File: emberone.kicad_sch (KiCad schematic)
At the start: 2 parts, among them J1 Screw Terminal, J2 Screw Terminal

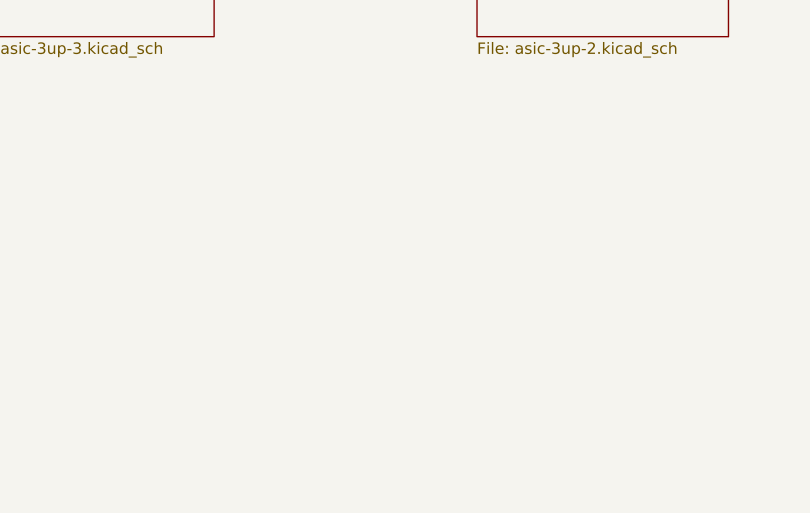
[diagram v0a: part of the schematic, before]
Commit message: added the heatsink mounting holes
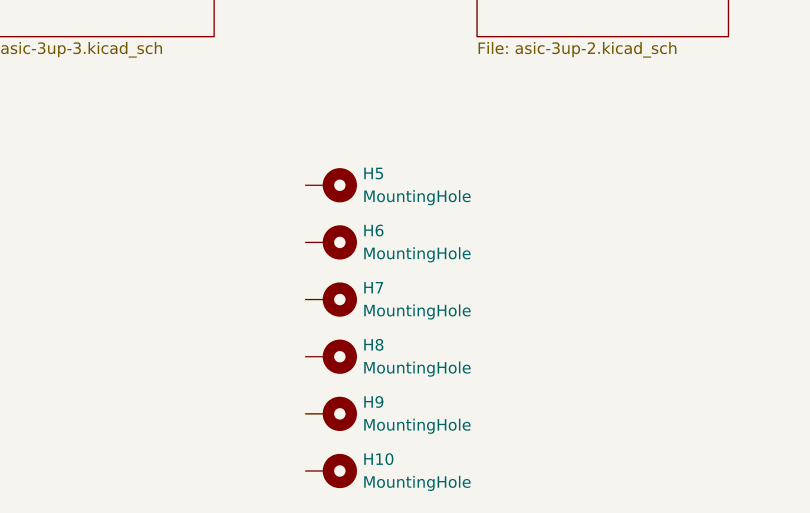
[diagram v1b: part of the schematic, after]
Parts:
- added H10, H5, H6, H7, H8, H9: MountingHole, MountingHole:MountingHole_3.2mm_M3_Pad, symbol Mechanical:MountingHole_Pad

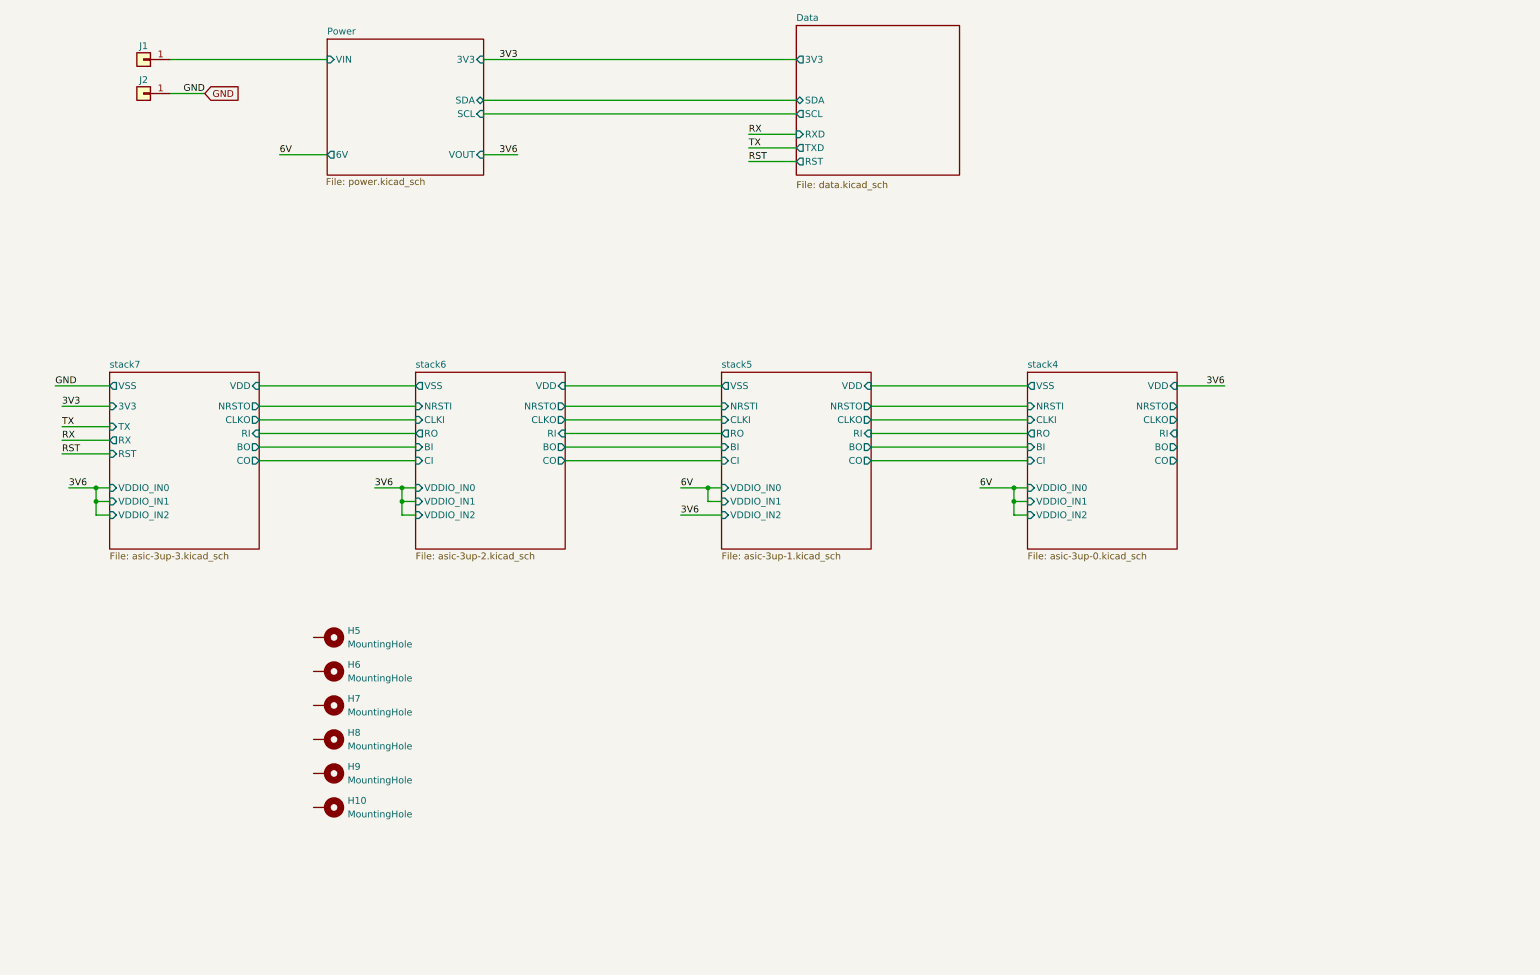
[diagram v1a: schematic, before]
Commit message: Switched to 5V for VDDIO LDO input.. cleaned up RP2040 circuit. Need to place and route testpoints
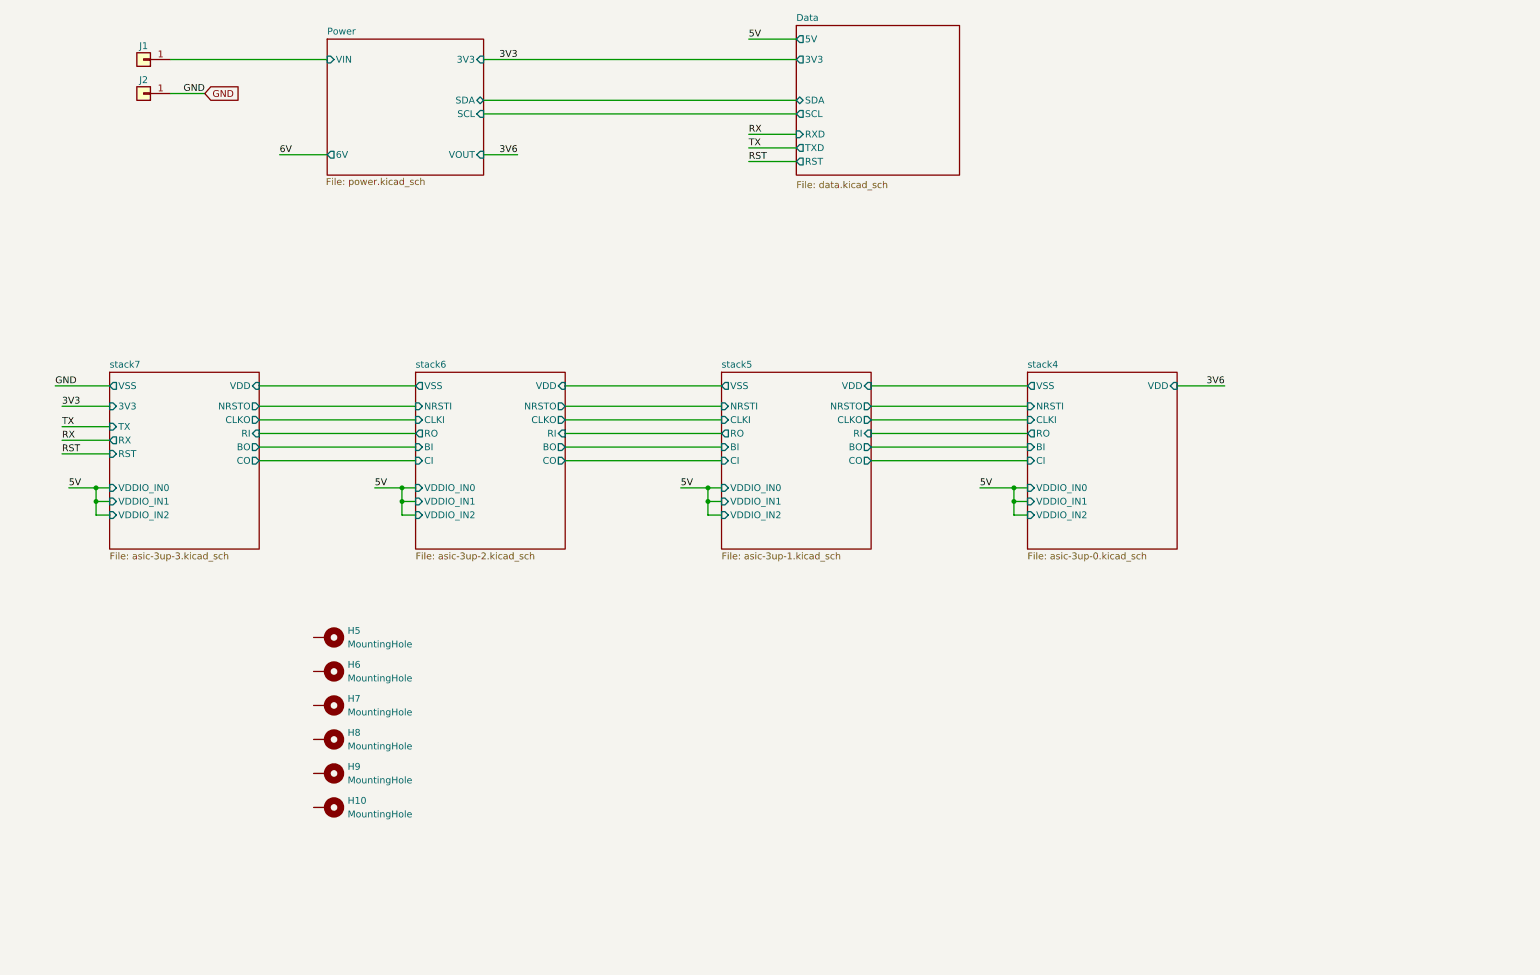
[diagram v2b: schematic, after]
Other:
- sheet Data ports: added 5V; removed none
- sheet stack4 ports: added none; removed BO, CLKO, CO, NRSTO, RI
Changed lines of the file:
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@@
+	)
+	(junction
+		(at 222.25 165.1)
+		(diameter 0)
+		(color 0 0 0 0)
 	)
 	(junction
@@
 	(wire
 		(pts
+			(xy 224.79 167.64) (xy 222.25 167.64)
+		)
+		(stroke
+			(width 0)
+			(type default)
+		)
+	)
+	(wire
+		(pts
 			(xy 229.87 101.6) (xy 238.76 101.6)
 		)
@@
 	(wire
 		(pts
+			(xy 222.25 167.64) (xy 222.25 165.1)
+		)
+		(stroke
+			(width 0)
+			(type default)
+		)
+	)
+	(wire
+		(pts
 			(xy 101.6 156.21) (xy 110.49 156.21)
 		)
@@
 	(wire
 		(pts
+			(xy 229.87 78.74) (xy 238.76 78.74)
+		)
+		(stroke
+			(width 0)
+			(type default)
+		)
+	)
+	(wire
+		(pts
 			(xy 121.92 82.55) (xy 151.13 82.55)
 		)
@@
 	(wire
 		(pts
-			(xy 217.17 167.64) (xy 224.79 167.64)
-		)
-		(stroke
-			(width 0)
-			(type default)
-		)
-	)
-	(wire
-		(pts
 			(xy 107.95 162.56) (xy 110.49 162.56)
 		)
@@
 		)
 	)
-	(label "GND"
-		(at 128.27 88.9 180)
+	(label "5V"
+		(at 160.02 162.56 0)
 		(fields_autoplaced yes)
 		(effects
@@
 				(size 1.27 1.27)
 			)
-			(justify right bottom)
-		)
-	)
-	(label "6V"
-		(at 217.17 162.56 0)
+			(justify left bottom)
+		)
+	)
+	(label "GND"
+		(at 128.27 88.9 180)
 		(fields_autoplaced yes)
 		(effects
@@
 				(size 1.27 1.27)
 			)
-			(justify left bottom)
+			(justify right bottom)
 		)
 	)
@@
 		)
 	)
-	(label "3V6"
-		(at 217.17 167.64 0)
+	(label "5V"
+		(at 102.87 162.56 0)
 		(fields_autoplaced yes)
 		(effects
@@
 		)
 	)
-	(label "3V6"
-		(at 160.02 162.56 0)
+	(label "TX"
+		(at 229.87 99.06 0)
 		(fields_autoplaced yes)
 		(effects
@@
 		)
 	)
-	(label "TX"
-		(at 229.87 99.06 0)
+	(label "5V"
+		(at 217.17 162.56 0)
 		(fields_autoplaced yes)
 		(effects
@@
 		)
 	)
-	(label "TX"
-		(at 101.6 151.13 0)
+	(label "5V"
+		(at 273.05 162.56 0)
 		(fields_autoplaced yes)
 		(effects
@@
 		)
 	)
-	(label "RX"
-		(at 101.6 153.67 0)
+	(label "TX"
+		(at 101.6 151.13 0)
 		(fields_autoplaced yes)
 		(effects
@@
 		)
 	)
-	(label "3V6"
-		(at 318.77 143.51 180)
+	(label "RX"
+		(at 101.6 153.67 0)
 		(fields_autoplaced yes)
 		(effects
@@
 				(size 1.27 1.27)
 			)
-			(justify right bottom)
-		)
-	)
-	(label "3V3"
-		(at 101.6 147.32 0)
+			(justify left bottom)
+		)
+	)
+	(label "3V6"
+		(at 318.77 143.51 180)
 		(fields_autoplaced yes)
 		(effects
@@
 				(size 1.27 1.27)
 			)
-			(justify left bottom)
-		)
-	)
-	(label "3V6"
-		(at 186.69 100.33 180)
+			(justify right bottom)
+		)
+	)
+	(label "3V3"
+		(at 101.6 147.32 0)
 		(fields_autoplaced yes)
 		(effects
@@
 				(size 1.27 1.27)
 			)
-			(justify right bottom)
+			(justify left bottom)
 		)
 	)
 	(label "3V6"
-		(at 102.87 162.56 0)
+		(at 186.69 100.33 180)
 		(fields_autoplaced yes)
 		(effects
@@
 				(size 1.27 1.27)
 			)
-			(justify left bottom)
-		)
-	)
-	(label "6V"
-		(at 273.05 162.56 0)
+			(justify right bottom)
+		)
+	)
+	(label "5V"
+		(at 229.87 78.74 0)
 		(fields_autoplaced yes)
 		(effects
@@
 			)
 		)
-		(pin "NRSTO" output
-			(at 309.88 147.32 0)
-			(effects
-				(font
-					(size 1.27 1.27)
-				)
-				(justify right)
-			)
-		)
-		(pin "CLKO" output
-			(at 309.88 149.86 0)
-			(effects
-				(font
-					(size 1.27 1.27)
-				)
-				(justify right)
-			)
-		)
-		(pin "RI" input
-			(at 309.88 152.4 0)
-			(effects
-				(font
-					(size 1.27 1.27)
-				)
-				(justify right)
-			)
-		)
-		(pin "BO" output
-			(at 309.88 154.94 0)
-			(effects
-				(font
-					(size 1.27 1.27)
-				)
-				(justify right)
-			)
-		)
-		(pin "CO" output
-			(at 309.88 157.48 0)
-			(effects
-				(font
-					(size 1.27 1.27)
-				)
-				(justify right)
-			)
-		)
 		(pin "VDDIO_IN0" input
 			(at 281.94 162.56 180)
@@
 			(effects
 				(font
+					(size 1.27 1.27)
+				)
+				(justify left)
+			)
+		)
+		(pin "5V" output
+			(at 238.76 78.74 180)
+			(effects
+				(font

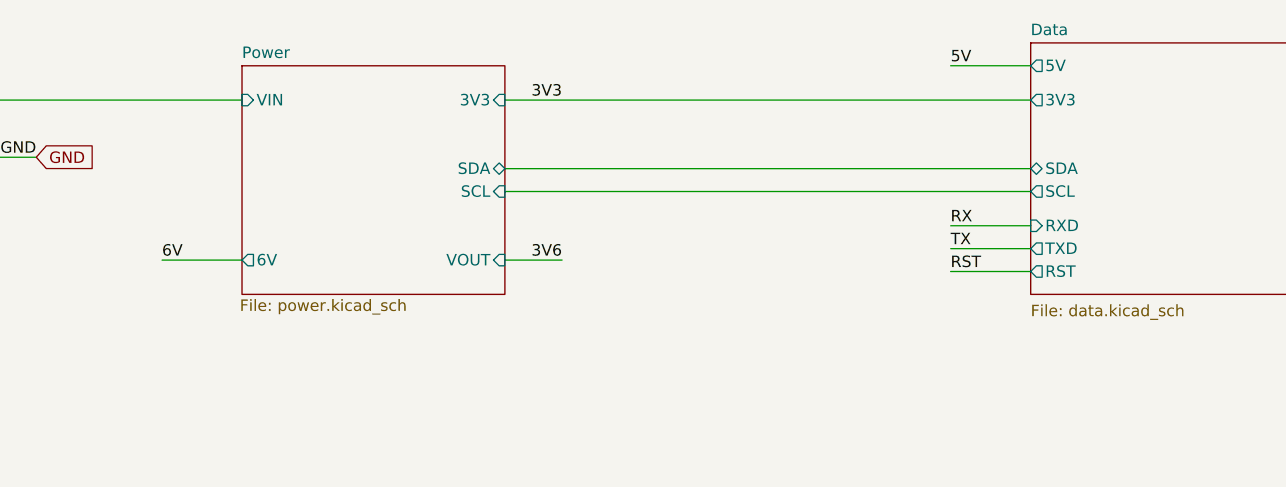
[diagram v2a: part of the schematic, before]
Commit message: added temp sensors. wired up (hopeful) vreg EN circuit. lots of LDO routing.
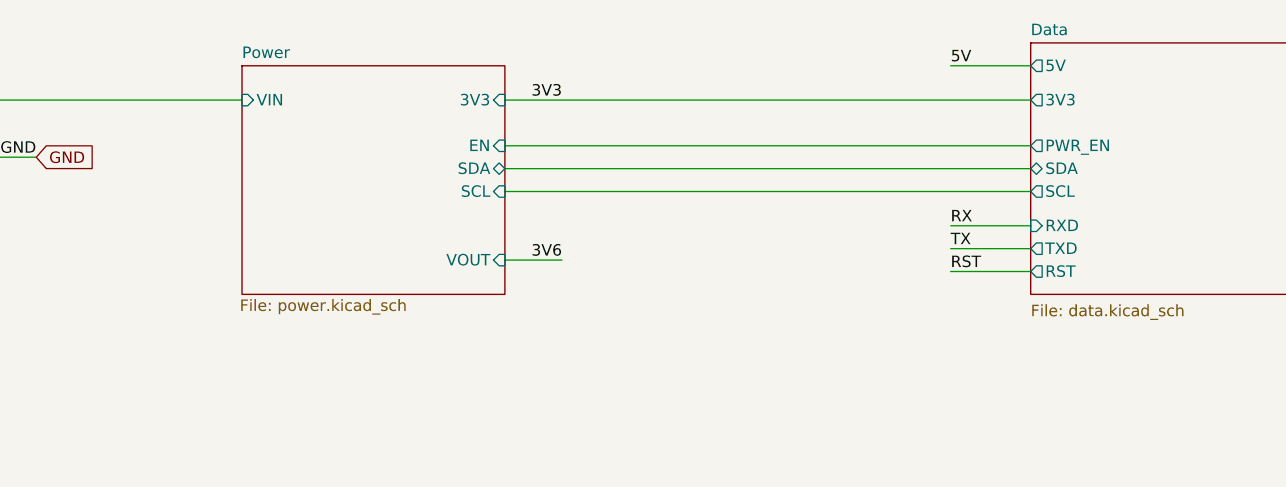
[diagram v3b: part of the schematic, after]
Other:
- sheet Data ports: added PWR_EN; removed none
- sheet Power ports: added EN; removed 6V
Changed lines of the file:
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@@
-	(wire
-		(pts
-			(xy 142.24 100.33) (xy 151.13 100.33)
-		)
-		(stroke
-			(width 0)
-			(type default)
-		)
-	)
 	(wire
 		(pts
@@
 		(pts
 			(xy 165.1 167.64) (xy 165.1 165.1)
+		)
+		(stroke
+			(width 0)
+			(type default)
+		)
+	)
+	(wire
+		(pts
+			(xy 180.34 87.63) (xy 238.76 87.63)
 		)
 		(stroke
@@
 	(label "5V"
 		(at 217.17 162.56 0)
-		(fields_autoplaced yes)
-		(effects
-			(font
-				(size 1.27 1.27)
-			)
-			(justify left bottom)
-		)
-	)
-	(label "6V"
-		(at 142.24 100.33 0)
 		(fields_autoplaced yes)
 		(effects
@@
 			)
 		)
-		(pin "6V" output
-			(at 151.13 100.33 180)
-			(effects
-				(font
-					(size 1.27 1.27)
-				)
-				(justify left)
+		(pin "EN" input
+			(at 180.34 87.63 0)
+			(effects
+				(font
+					(size 1.27 1.27)
+				)
+				(justify right)
 			)
 		)
@@
 			(effects
 				(font
+					(size 1.27 1.27)
+				)
+				(justify left)
+			)
+		)
+		(pin "PWR_EN" output
+			(at 238.76 87.63 180)
+			(effects
+				(font

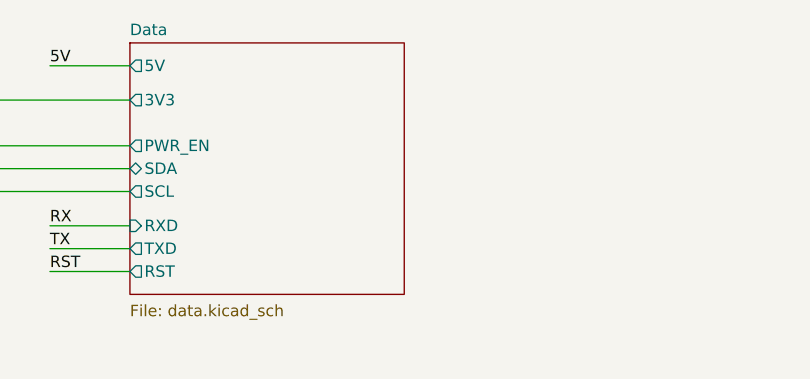
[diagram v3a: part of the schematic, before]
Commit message: all placed *almost* all routed
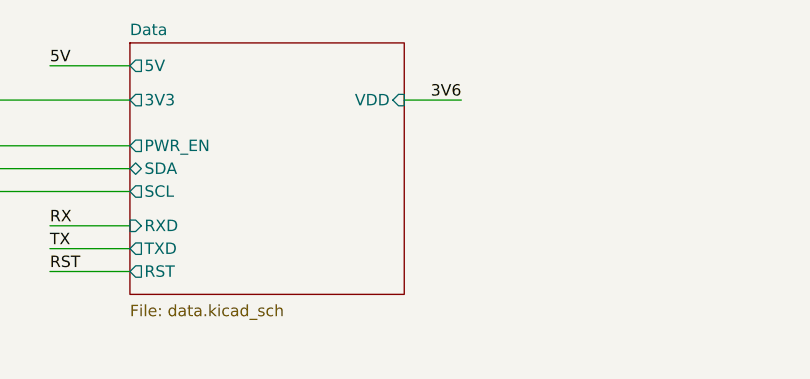
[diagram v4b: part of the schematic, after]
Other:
- sheet Data ports: added VDD; removed none
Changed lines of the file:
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@@
+	(wire
+		(pts
+			(xy 269.24 82.55) (xy 275.59 82.55)
+		)
+		(stroke
+			(width 0)
+			(type default)
+		)
+	)
 	(wire
 		(pts
@@
 			)
 			(justify left bottom)
+		)
+	)
+	(label "3V6"
+		(at 275.59 82.55 180)
+		(fields_autoplaced yes)
+		(effects
+			(font
+				(size 1.27 1.27)
+			)
+			(justify right bottom)
 		)
 	)
@@
 			)
 		)
+		(pin "VDD" input
+			(at 269.24 82.55 0)
+			(effects
+				(font
+					(size 1.27 1.27)
+				)
+				(justify right)
+			)
+		)

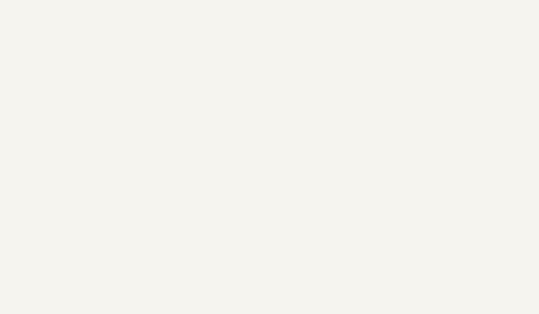
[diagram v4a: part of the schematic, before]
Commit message: DRC warnings cleanup. recentered logo
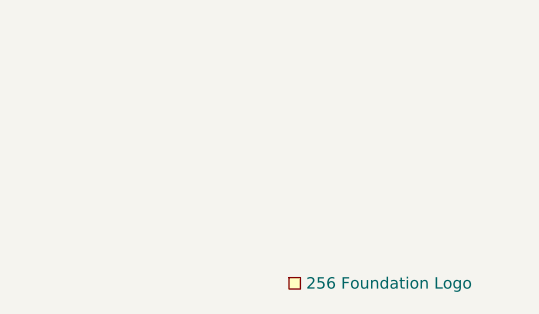
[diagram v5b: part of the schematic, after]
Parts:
- added U11: 256 Foundation Logo, emberone:256foundation_logo, symbol emberone:256logo
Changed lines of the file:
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@@
+	)
+	(symbol
+		(lib_id "emberone:256logo")
+		(at 350.52 250.19 0)
+		(unit 1)
+		(exclude_from_sim no)
+		(in_bom yes)
+		(on_board yes)
+		(dnp no)
+		(fields_autoplaced yes)
+		(property "Reference" "U11"
+			(at 350.52 250.19 0)
+			(effects
+				(font
+					(size 1.27 1.27)
+				)
+				(hide yes)
+			)
+		)
+		(property "Value" "256 Foundation Logo"
+			(at 351.79 250.1899 0)
+			(effects
+				(font
+					(size 1.27 1.27)
+				)
+				(justify left)
+			)
+		)
+		(property "Footprint" "emberone:256foundation_logo"
+			(at 350.52 250.19 0)
+			(effects
+				(font
+					(size 1.27 1.27)
+				)
+				(hide yes)
+			)
+		)
+		(property "Datasheet" ""
+			(at 350.52 250.19 0)
+			(effects
+				(font
+					(size 1.27 1.27)
+				)
+				(hide yes)
+			)
+		)
+		(property "Description" ""
+			(at 350.52 250.19 0)
+			(effects
+				(font
+					(size 1.27 1.27)
+				)
+				(hide yes)
+			)
+		)
+		(instances
+			(project ""
+				(path "/b036224c-4cdf-48cc-81df-19bc5283ebd2"
+					(reference "U11")
+					(unit 1)
+				)
+			)
+		)
 	)
 	(symbol

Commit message: generated updated gerbers
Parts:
- added H1, H2, H3, H4: MountingHole, MountingHole:MountingHole_3.5mm, symbol Mechanical:MountingHole
- added TP10, TP11, TP4, TP5: TestPoint, TestPoint:TestPoint_Pad_D1.0mm, symbol Connector:TestPoint
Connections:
- net GND: now also TP11.1
- net RST: now also TP10.1
- net RX: now also TP5.1
- net TX: now also TP4.1
- no-connect marks 0 -> 6

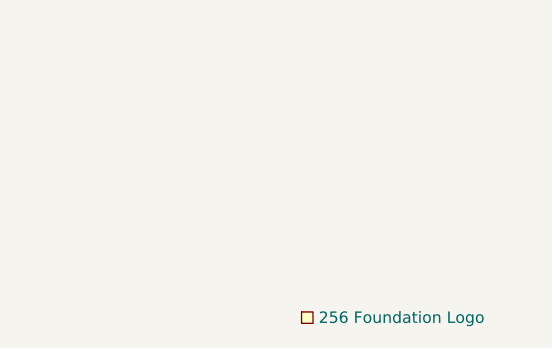
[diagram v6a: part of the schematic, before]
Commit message: added 70x90 heatsink model
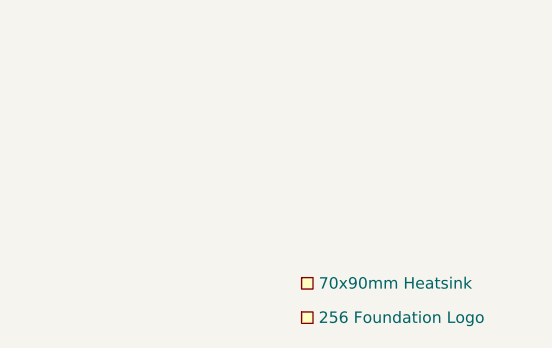
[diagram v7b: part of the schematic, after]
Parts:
- added U12: 70x90mm Heatsink, emberone:70x90mm_heatsink, symbol emberone:70x90_heatsink
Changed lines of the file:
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@@
+	)
+	(symbol
+		(lib_id "emberone:70x90_heatsink")
+		(at 350.52 246.38 0)
+		(unit 1)
+		(exclude_from_sim no)
+		(in_bom yes)
+		(on_board yes)
+		(dnp no)
+		(fields_autoplaced yes)
+		(property "Reference" "U12"
+			(at 350.52 246.38 0)
+			(effects
+				(font
+					(size 1.27 1.27)
+				)
+				(hide yes)
+			)
+		)
+		(property "Value" "70x90mm Heatsink"
+			(at 351.79 246.3799 0)
+			(effects
+				(font
+					(size 1.27 1.27)
+				)
+				(justify left)
+			)
+		)
+		(property "Footprint" "emberone:70x90mm_heatsink"
+			(at 350.266 249.936 0)
+			(effects
+				(font
+					(size 1.27 1.27)
+				)
+				(hide yes)
+			)
+		)
+		(property "Datasheet" ""
+			(at 350.52 246.38 0)
+			(effects
+				(font
+					(size 1.27 1.27)
+				)
+				(hide yes)
+			)
+		)
+		(property "Description" ""
+			(at 350.52 246.38 0)
+			(effects
+				(font
+					(size 1.27 1.27)
+				)
+				(hide yes)
+			)
+		)
+		(instances
+			(project ""
+				(path "/b036224c-4cdf-48cc-81df-19bc5283ebd2"
+					(reference "U12")
+					(unit 1)
+				)
+			)
+		)
 	)
 	(symbol
